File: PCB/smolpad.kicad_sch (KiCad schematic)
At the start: 21 parts, among them SW1 SW_Push_45deg, SW10 RotaryEncoder_Switch_MP, SW2 SW_Push_45deg, SW3 SW_Push_45deg, SW4 SW_Push_45deg, SW5 SW_Push_45deg, SW6 SW_Push_45deg, SW7 SW_Push_45deg, SW8 SW_Push_45deg, SW9 SW_Push_45deg, U1 MOUDLE-SEEEDUINO-XIAO, U2 ER_OLEDM0.91_1x-I2C

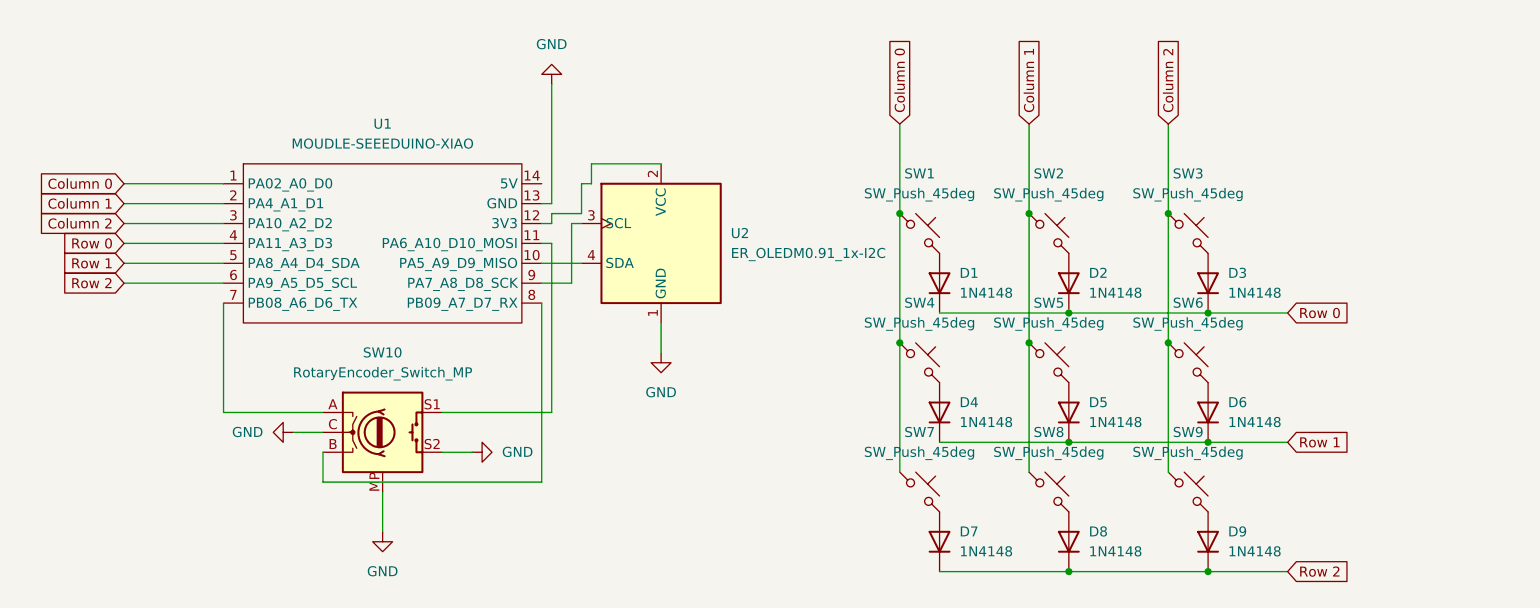
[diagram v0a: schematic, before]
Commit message: changed footprints
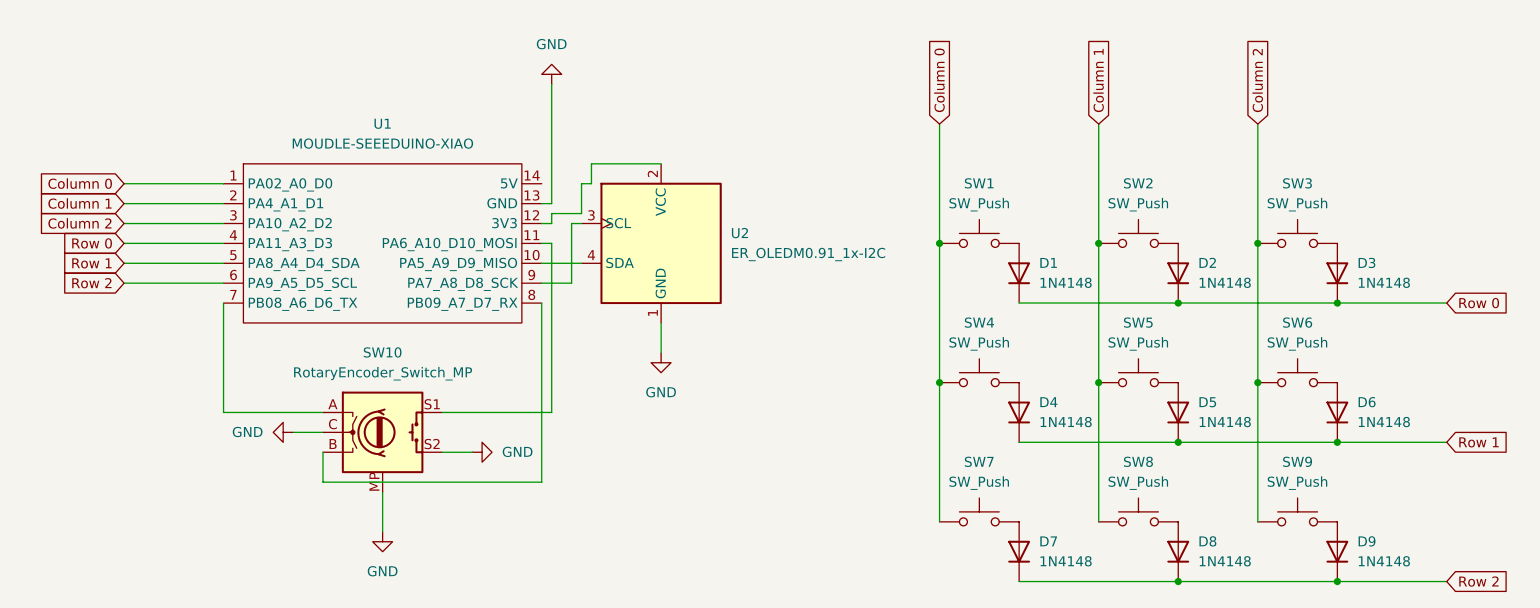
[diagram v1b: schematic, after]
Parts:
- removed SW1, SW2, SW3, SW4, SW5, SW6, SW7, SW8, SW9: SW_Push_45deg, Button_Switch_Keyboard:SW_Cherry_MX_1.00u_Plate, symbol Switch:SW_Push_45deg
- added SW1, SW2, SW3, SW4, SW5, SW6, SW7, SW8, SW9: SW_Push, Button_Switch_Keyboard:SW_Cherry_MX_1.00u_PCB, symbol Switch:SW_Push
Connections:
- net Column 0: now also SW1.1, SW4.1, SW7.1
- net Column 1: now also SW2.1, SW5.1, SW8.1
- net Column 2: now also SW3.1, SW6.1, SW9.1
- net at D7.2 (A): now also SW7.2
- net at D4.2 (A): now also SW4.2
- net at D5.2 (A): now also SW5.2
- net at D2.2 (A): now also SW2.2
- net at D3.2 (A): now also SW3.2
- net at D1.2 (A): now also SW1.2
- net at D9.2 (A): now also SW9.2
- net at D8.2 (A): now also SW8.2
- net at D6.2 (A): now also SW6.2
